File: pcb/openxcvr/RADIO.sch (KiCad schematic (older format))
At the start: 0 parts

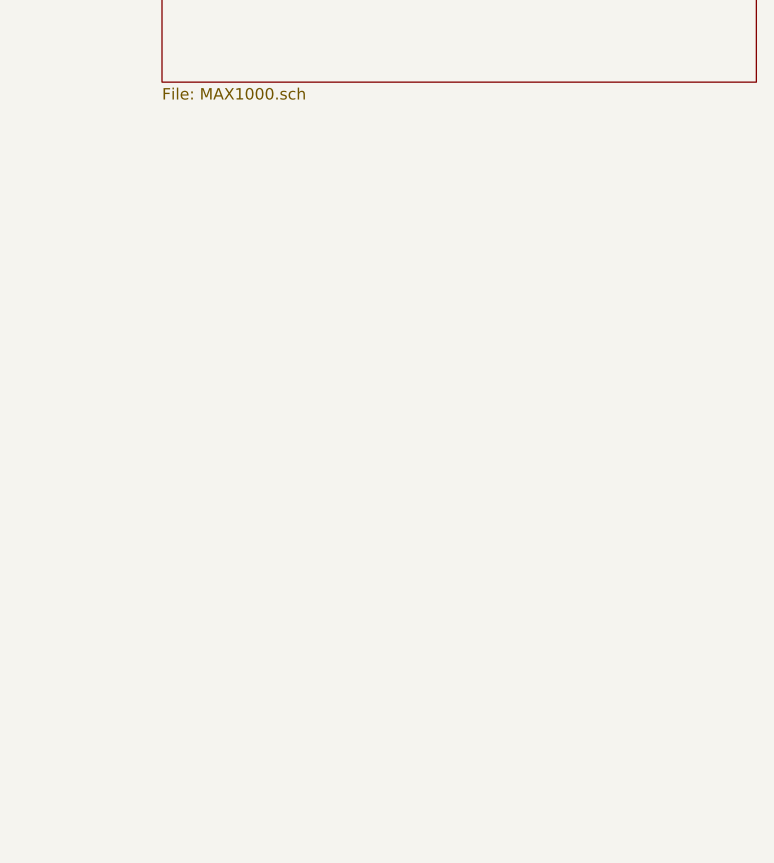
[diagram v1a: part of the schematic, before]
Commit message: Add eeprom load store capability
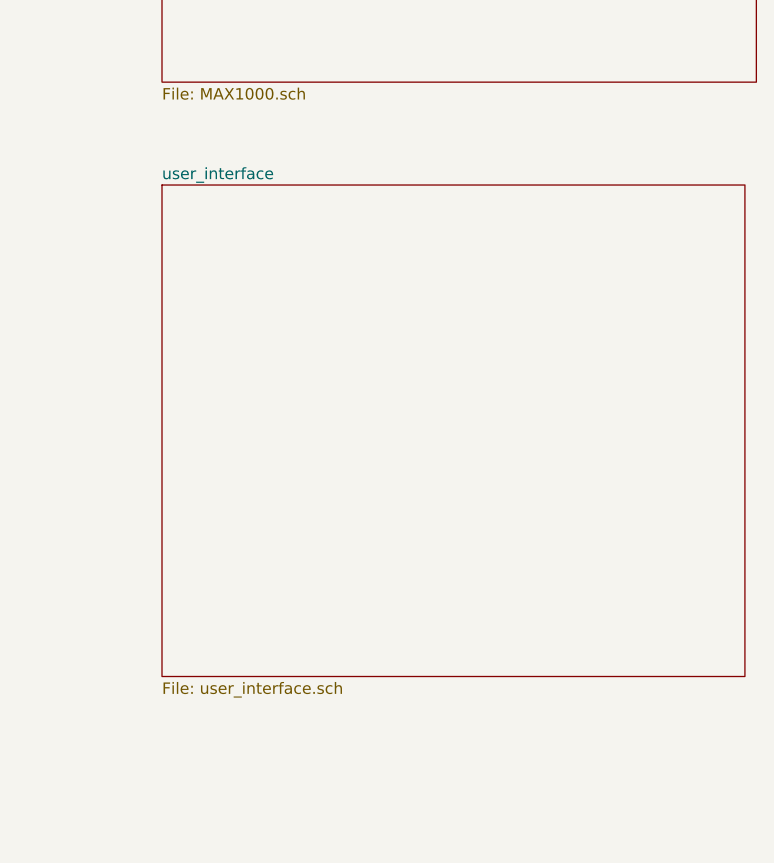
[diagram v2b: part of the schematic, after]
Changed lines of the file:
@@
 $Descr A4 11693 8268
 encoding utf-8
-Sheet 1 6
+Sheet 1 7
 Title "Open XCVR"
 Date "2020-01-26"
@@
 F1 "MAX1000.sch" 50
 $EndSheet
+$Sheet
+S 6850 4000 2550 2150
+U 5EA9DF7D
+F0 "user_interface" 50
+F1 "user_interface.sch" 50
+$EndSheet
 $EndSCHEMATC

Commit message: Review schematic and PCB layout
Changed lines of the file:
@@
 Sheet 1 7
 Title "Open XCVR"
-Date "2020-01-26"
-Rev "0.1"
+Date "2020-06-14"
+Rev "0.2"
 Comp "Jon Dawson"
 Comment1 ""
@@
 $EndSheet
 $Sheet
+S 650  6550 1050 1100
+U 5E35BCF5
+F0 "RX mixer" 50
+F1 "rx_mixer.sch" 50
+$EndSheet
+$Sheet
 S 1000 1000 1050 1050
 U 5E371E22
-F0 "AUDIO" 50
+F0 "audio" 50
 F1 "audio.sch" 50
-$EndSheet
-$Sheet
-S 650  6550 1050 1100
-U 5E35BCF5
-F0 "RX_MIXER" 50
-F1 "rx_mixer.sch" 50
 $EndSheet
 $Sheet
 S 2200 3850 1900 1300
 U 5E421DE9
-F0 "bandpass" 50
+F0 "bandpass filters" 50
 F1 "bandpass.sch" 50
 $EndSheet
@@
 S 6850 4000 2550 2150
 U 5EA9DF7D
-F0 "user_interface" 50
+F0 "user interface" 50
 F1 "user_interface.sch" 50
 $EndSheet
